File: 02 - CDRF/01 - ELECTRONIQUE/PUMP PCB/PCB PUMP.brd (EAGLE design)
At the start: 25 x 25 mm, 13 parts, among them J3 PWRPAD2-5MM, J4 PWRPAD2-5MM, Q1 FDN360P, Q2 FDN360P

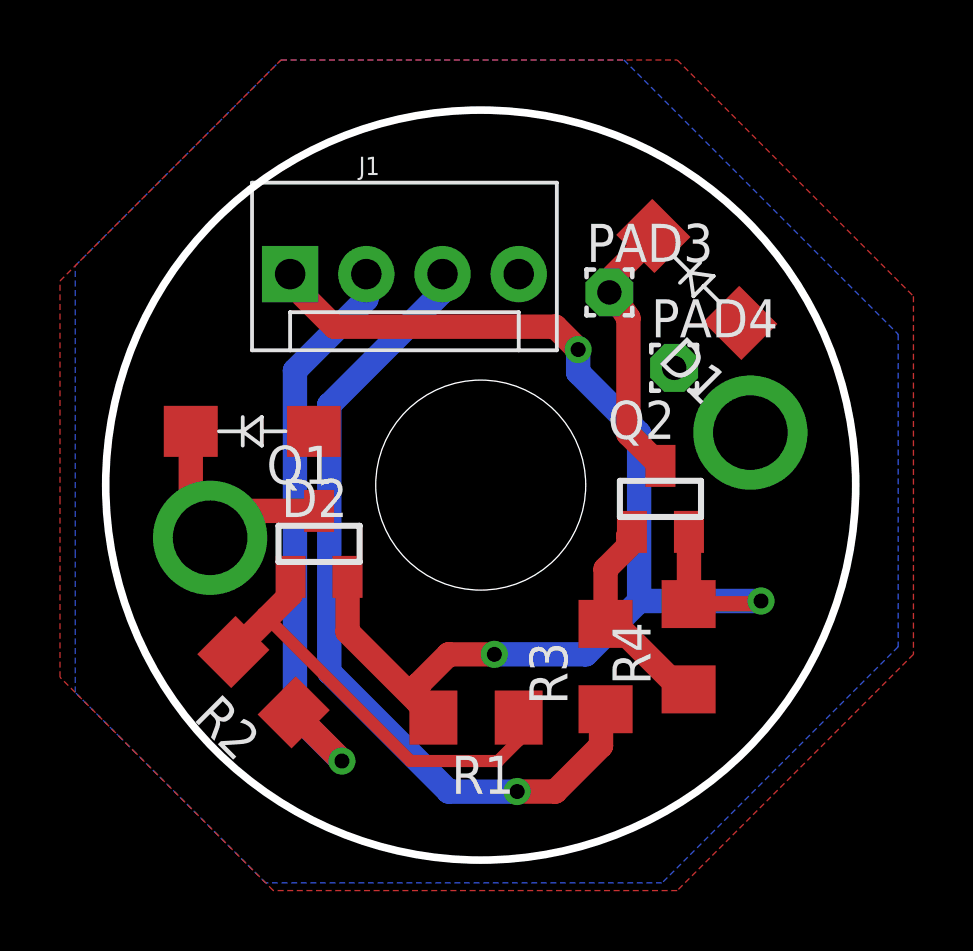
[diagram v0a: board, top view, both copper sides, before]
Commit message: Update
Change P-MOSFET by N-MOSFET
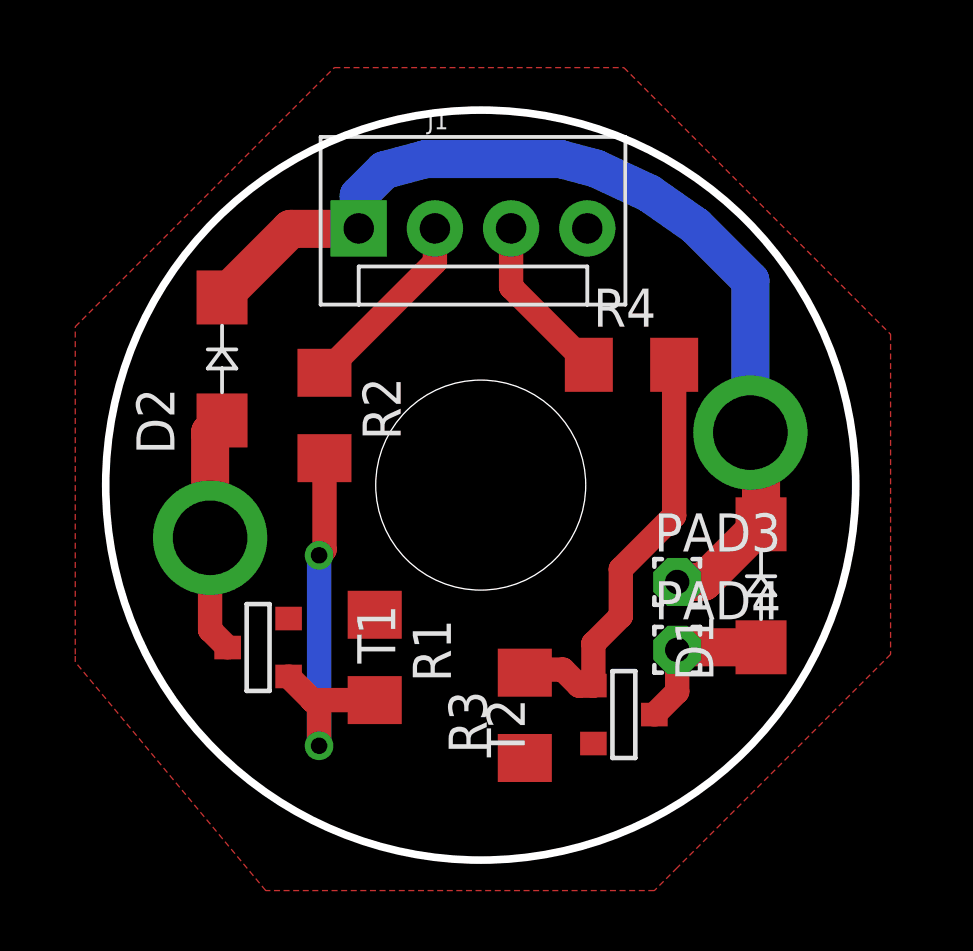
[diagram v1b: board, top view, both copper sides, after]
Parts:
- removed Q1, Q2: FDN360P, transistor-power:SUPER-SOT3
- added T1, T2: (no value), fab:SOT-23
- R3: value 1K -> 10k
- R4: value 10k -> 1K
- moved D1 10.4 mm to (21.8, 9.14), turned to 90 degrees
- moved PAD3 9.91 mm to (19.1, 9.27)
- moved R4 9.59 mm to (17.5, 16.5), turned to 0 degrees
- moved PAD4 9.40 mm to (19.1, 7.01)
- moved R2 9.12 mm to (7.29, 14.8), turned to 270 degrees
- moved R1 3.93 mm to (8.97, 6.76), turned to 270 degrees
- moved R3 3.14 mm to (14.0, 4.83)
- moved J1 2.75 mm to (8.43, 21.1)
- moved D2 2.61 mm to (3.88, 16.7), turned to 90 degrees
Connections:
- removed net N$5: D2.K, J3.P$1, Q1.3
- removed net N$8: D1.K, PAD3.1, Q2.3
- new net N$2: D2.A, J3.P$1, T1.1
- new net N$3: R1.2, R2.2, T1.3
- net +5V: now also D1.K, D2.K, J4.P$1, PAD3.1; no longer Q1.2, Q2.2, R1.2, R4.2
- net EV: now also R4.1; no longer R3.1
- net GND: now also R1.1, R3.1, T1.2, T2.2; no longer D1.A, D2.A, J4.P$1, PAD4.1
- net N$1: now also D1.A, PAD4.1, T2.1; no longer Q2.1, R3.2, R4.1
- net N$4: now also R3.2, R4.2, T2.3; no longer Q1.1, R1.1, R2.2
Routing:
- net EV: track 27.5 -> 5.62 mm, vias 1 -> 0
- net N$3: track 0.00 -> 14.5 mm, vias 0 -> 2
- net PUMP: track 20.2 -> 6.34 mm, vias 1 -> 0
- net +5V: track 44.6 -> 33.5 mm, vias 3 -> 0
- net N$8: track 8.93 -> 0.00 mm
- net N$2: track 0.00 -> 7.98 mm
- net N$5: track 7.82 -> 0.00 mm
- net N$1: track 7.10 -> 5.30 mm
- removed copper zone on layer 16, net GND
